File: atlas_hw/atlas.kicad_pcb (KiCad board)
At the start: 2 copper layers, 200 parts, among them J1 USB_C_Receptacle_USB2.0, J10 PSP_LCD, J2 DEBUG_STM, J3 PSP_TOUCH, J4 DEBUG_NRF, J5 CELL_THERM, J6 CELL_BARE, J7 AUX_THERM, J8 Micro_SD_Card_Det, J9 PSP_LCD_BL, Q1 Q_NMOS_DGS, Q2 Q_NMOS_DGS, Q3 Q_NMOS_DGS, Q4 Q_NMOS_DGS, Q5 Q_NMOS_DGS, SW1 SReset, SW2 Power, SW3 ResetSTM, SW4 ResetNRF, U1 STM32H723VITx, U10 BQ25611D, U11 STM6601CA2BDM6F, U12 BGA725L6, U13 LSF0108, U14 NPP600SNADJ, U15 TPS61073, U16 PAM2841, U17 NX3L1T3157, U2 W957A8MFYA5I, U3 MCP1811B, U4 TLV62569DBV, U5 nRF52810-QCxx, U6 LC709203F, U7 Teseo-LIV3F, U8 MS5637, U9 MC6470, Y1 16M, Y2 32k, Y3 32M, Y4 32k

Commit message: started layout
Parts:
- removed R45, R48, R49, R50, R51, R52, R53: NP, Resistor_SMD:R_0402_1005Metric
- removed U17: NX3L1T3157, Package_TO_SOT_SMD:SOT-886
- added RN5: R_Pack04, Resistor_SMD:R_Array_Concave_4x0402, F.Cu at (125.2, 40.9)
- added RN6: R_Pack04, Resistor_SMD:R_Array_Concave_4x0402, F.Cu at (128.3, 40.9)
- AE1: footprint Inductor_SMD:L_1206_3216Metric -> Resistor_SMD:R_1206_3216Metric
- J3, RN1, RN2, RN3, RN4, U1, U7: moved to B.Cu
- U12: value BGA725L6 -> BGU7007; footprint atlas:TSLP-6-2 -> atlas:6-XSON_1.5x1.0mm_0.5mm
- Y1, Y3: footprint Crystal:Crystal_SMD_2016-4Pin_2.0x1.6mm -> Crystal:Crystal_SMD_3225-4Pin_3.2x2.5mm
- Y2, Y4: footprint Crystal:Crystal_SMD_2012-2Pin_2.0x1.2mm -> Crystal:Crystal_SMD_3225-4Pin_3.2x2.5mm
- moved J8 154.1 mm to (257.3, 137.4), turned to 90 degrees
- moved U2 140.3 mm to (255.4, 124.7), turned to 270 degrees
- moved U10 137.7 mm to (233.8, 160.9)
- moved U5 129.4 mm to (252.9, 168.7), turned to 180 degrees
- moved J1 125.6 mm to (230.9, 175.2)
- moved AE2 124.4 mm to (206.6, 167.2), turned to 180 degrees
- moved U1 109.7 mm to (240.4, 129.8)
- moved U7 104.9 mm to (210.0, 157.8), turned to 180 degrees
- moved U13 96.7 mm to (241.1, 133.7)
- moved RN1 65.5 mm to (219.3, 136.7), turned to 0 degrees
- moved J10 64.6 mm to (223.1, 129.7)
- moved RN2 42.3 mm to (219.3, 132.7)
- moved RN3 39.3 mm to (219.3, 128.7)
- moved RN4 35.1 mm to (219.3, 125.2)
- moved J3 32.9 mm to (122.6, 139.0), turned to 270 degrees
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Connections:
- U12 pad 2: /GPS_VCC_RF -> GND
- U12 pad 3: Net-(F1-Pad1) -> Net-(L8-Pad1)
- U12 pad 4: GND -> /GPS_VCC_RF
- U12 pad 5: Net-(L8-Pad1) -> /GPS_ANT_OFF
- U12 pad 6: /GPS_ANT_OFF -> Net-(F1-Pad1)
- U6 pad 7: (no net) -> /I2C1_SCL_SYSTEM
- U6 pad 8: (no net) -> /I2C1_SCL_SYSTEM
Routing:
- net /SD_D1: track 0.00 -> 26.0 mm
- net /SD_D0: track 0.00 -> 24.5 mm
- net /SD_CLK: track 0.00 -> 24.2 mm
- net /OCTOSPIM_P1_NPLK: track 0.00 -> 22.2 mm, vias 0 -> 1
- net /SD_CMD: track 0.00 -> 21.4 mm
- net /SD_D3: track 0.00 -> 21.1 mm
- net /SD_D2: track 0.00 -> 20.9 mm
- net /OCTOSPIM_P1_NPS: track 0.00 -> 13.4 mm, vias 0 -> 1
- net /OCTOSPIM_P1_IO7: track 0.00 -> 11.9 mm, vias 0 -> 1
- net /OCTOSPIM_P1_IO6: track 0.00 -> 11.0 mm, vias 0 -> 1
- net /OCTOSPIM_P1_CLK: track 0.00 -> 10.7 mm, vias 0 -> 1
- net /OCTOSPIM_P1_IO5: track 0.00 -> 10.3 mm, vias 0 -> 1
- net /SDMMC1_D2: track 0.00 -> 8.88 mm, vias 0 -> 1
- net /OCTOSPIM_P1_IO4: track 0.00 -> 8.66 mm, vias 0 -> 1
- net /OCTOSPIM_P1_DQS: track 0.00 -> 8.44 mm, vias 0 -> 1
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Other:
- board outline added: 71 x 73.4 mm

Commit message: gps and other layout
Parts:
- removed J6: CELL_BARE, Connector_JST:JST_GH_SM02B-GHS-TB_1x02-1MP_P1.25mm_Horizontal
- removed J7: AUX_THERM, Connector_JST:JST_GH_SM02B-GHS-TB_1x02-1MP_P1.25mm_Horizontal
- C43, C45, C46, F1, J5, R12, R13, R14, R15, RN5, RN6, U12: moved to B.Cu
- J1: footprint Connector_USB:USB_C_Receptacle_Amphenol_12401548E4-2A -> Connector_USB:USB_C_Receptacle_Amphenol_12401610E4-2A
- L8: footprint Inductor_SMD:L_0603_1608Metric -> Inductor_SMD:L_0402_1005Metric; moved to B.Cu
- moved RN5 154.6 mm to (242.6, 141.6), turned to 180 degrees
- moved RN6 154.0 mm to (242.6, 144.1), turned to 180 degrees
- moved U6 136.3 mm to (255.3, 161.9), turned to 180 degrees
- moved J5 125.9 mm to (245.3, 152.6)
- moved C31 112.3 mm to (255.3, 158.5), turned to 180 degrees
- moved C46 110.8 mm to (203.6, 168.1), turned to 180 degrees
- moved C27 105.3 mm to (232.8, 168.6)
- moved L3 99.2 mm to (143.8, 174.0), turned to 180 degrees
- moved R13 95.0 mm to (232.7, 171.1)
- moved R14 94.9 mm to (231.4, 166.3), turned to 270 degrees
- moved R12 93.1 mm to (228.9, 171.1)
- moved R16 93.0 mm to (231.4, 166.3), turned to 270 degrees
- moved C13 92.7 mm to (147.3, 169.4)
- moved R17 91.4 mm to (230.4, 166.3), turned to 270 degrees
- moved L2 91.3 mm to (208.0, 128.8), turned to 90 degrees
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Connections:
- J10 pad 1: GND -> Net-(J10-Pad1)
- J10 pad 10: /LTDC_R5 -> /LTDC_DE
- J10 pad 11: /LTDC_R6 -> /LTDC_CK
- J10 pad 12: /LTDC_R7 -> GND
- J10 pad 13: /LTDC_G4 -> /LTDC_B7
- J10 pad 14: /LTDC_G5 -> /LTDC_B6
- J10 pad 15: /LTDC_G6 -> /LTDC_B5
- J10 pad 16: /LTDC_G7 -> /LTDC_B4
- J10 pad 17: /LTDC_G4 -> /LTDC_B7
- J10 pad 18: /LTDC_G5 -> /LTDC_B6
- J10 pad 19: /LTDC_G6 -> /LTDC_B5
- J10 pad 2: GND -> Net-(J10-Pad2)
- J10 pad 20: /LTDC_G7 -> /LTDC_B4
- J10 pad 21: /LTDC_B4 -> /LTDC_G7
- J10 pad 22: /LTDC_B5 -> /LTDC_G6
- J10 pad 23: /LTDC_B6 -> /LTDC_G5
- J10 pad 24: /LTDC_B7 -> /LTDC_G4
- J10 pad 25: /LTDC_B4 -> /LTDC_G7
- J10 pad 26: /LTDC_B5 -> /LTDC_G6
- J10 pad 27: /LTDC_B6 -> /LTDC_G5
- J10 pad 28: /LTDC_B7 -> /LTDC_G4
- J10 pad 29: GND -> /LTDC_R7
- J10 pad 3: Net-(C54-Pad1) -> Net-(J10-Pad3)
- J10 pad 30: /LTDC_CK -> /LTDC_R6
- J10 pad 31: /LTDC_DE -> /LTDC_R5
- J10 pad 32: /LTDC_HS -> /LTDC_R4
- J10 pad 33: /LTDC_VS -> /LTDC_R7
- J10 pad 34: Net-(J10-Pad34) -> /LTDC_R6
- J10 pad 35: Net-(C51-Pad1) -> /LTDC_R5
- J10 pad 36: Net-(J10-Pad36) -> /LTDC_R4
- J10 pad 37: Net-(J10-Pad37) -> Net-(C54-Pad1)
- J10 pad 38: Net-(J10-Pad38) -> Net-(C54-Pad1)
- J10 pad 39: Net-(J10-Pad39) -> GND
- J10 pad 4: Net-(C54-Pad1) -> Net-(J10-Pad4)
- J10 pad 40: Net-(J10-Pad40) -> GND
- J10 pad 5: /LTDC_R4 -> Net-(J10-Pad5)
- J10 pad 6: /LTDC_R5 -> Net-(C51-Pad1)
- J10 pad 7: /LTDC_R6 -> Net-(J10-Pad7)
- J10 pad 8: /LTDC_R7 -> /LTDC_VS
- J10 pad 9: /LTDC_R4 -> /LTDC_HS
- R82 pad 2: Net-(J10-Pad38) -> Net-(J10-Pad3)
- R83 pad 2: Net-(J10-Pad39) -> Net-(J10-Pad2)
- R84 pad 2: Net-(J10-Pad40) -> Net-(J10-Pad1)
- RN1 pad 1: GND -> /LTDC_R4
- RN1 pad 2: GND -> /LTDC_R5
- RN1 pad 3: GND -> /LTDC_R6
- RN1 pad 4: GND -> /LTDC_R7
- RN1 pad 5: /LTDC_R7 -> GND
- RN1 pad 6: /LTDC_R6 -> GND
- RN1 pad 7: /LTDC_R5 -> GND
- RN1 pad 8: /LTDC_R4 -> GND
- RN2 pad 1: GND -> /LTDC_G4
- RN2 pad 2: GND -> /LTDC_G5
- RN2 pad 3: GND -> /LTDC_G6
- RN2 pad 4: GND -> /LTDC_G7
- RN2 pad 5: /LTDC_G7 -> GND
- RN2 pad 6: /LTDC_G6 -> GND
- RN2 pad 7: /LTDC_G5 -> GND
- RN2 pad 8: /LTDC_G4 -> GND
- RN3 pad 1: GND -> /LTDC_B4
- RN3 pad 2: GND -> /LTDC_B5
- RN3 pad 3: GND -> /LTDC_B6
- RN3 pad 4: GND -> /LTDC_B7
- RN3 pad 5: /LTDC_B7 -> GND
- RN3 pad 6: /LTDC_B6 -> GND
- RN3 pad 7: /LTDC_B5 -> GND
- RN3 pad 8: /LTDC_B4 -> GND
- RN4 pad 1: GND -> /LTDC_CK
- RN4 pad 2: GND -> /LTDC_DE
- RN4 pad 3: GND -> /LTDC_HS
- RN4 pad 4: GND -> /LTDC_VS
- RN4 pad 5: /LTDC_VS -> GND
- RN4 pad 6: /LTDC_HS -> GND
- RN4 pad 7: /LTDC_DE -> GND
- RN4 pad 8: /LTDC_CK -> GND
- RN5 pad 1: /SDMMC1_D2 -> /SD_D2
- RN5 pad 2: /SDMMC1_D3 -> /SD_D3
- RN5 pad 3: /SDMMC1_CMD -> /SD_CMD
- RN5 pad 4: /SDMMC1_CK -> /SD_CLK
- RN5 pad 5: /SD_CLK -> /SDMMC1_CK
- RN5 pad 6: /SD_CMD -> /SDMMC1_CMD
- RN5 pad 7: /SD_D3 -> /SDMMC1_D3
- RN5 pad 8: /SD_D2 -> /SDMMC1_D2
- RN6 pad 1: /SDMMC1_D0 -> /SD_D0
- RN6 pad 2: /SDMMC1_D1 -> /SD_D1
- RN6 pad 7: /SD_D1 -> /SDMMC1_D1
- RN6 pad 8: /SD_D0 -> /SDMMC1_D0
- U6 pad : (no net) -> GND
- U7 pad 10: Net-(C43-Pad2) -> GND
- U7 pad 11: (no net) -> Net-(C43-Pad2)
- U7 pad 18: (no net) -> Net-(U7-Pad18)
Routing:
- net /LTDC_R5: track 0.00 -> 43.7 mm, vias 0 -> 4
- net /LTDC_R4: track 0.00 -> 41.6 mm, vias 0 -> 4
- net /LTDC_R6: track 0.00 -> 39.4 mm, vias 0 -> 4
- net /LTDC_B7: track 0.00 -> 38.7 mm, vias 0 -> 4
- net /LTDC_VS: track 0.00 -> 37.8 mm, vias 0 -> 4
- net /LTDC_G7: track 0.00 -> 37.1 mm, vias 0 -> 4
- net /LTDC_R7: track 0.00 -> 36.2 mm, vias 0 -> 4
- net /LTDC_HS: track 0.00 -> 36.2 mm, vias 0 -> 2
- net /LTDC_B5: track 0.00 -> 35.6 mm, vias 0 -> 4
- net /LTDC_G5: track 0.00 -> 35.6 mm, vias 0 -> 4
- net /LTDC_B4: track 0.00 -> 35.3 mm, vias 0 -> 4
- net /LTDC_G4: track 0.00 -> 35.1 mm, vias 0 -> 4
- net /LPUART1_TX_GPS: track 0.00 -> 34.9 mm
- net /LPUART1_RX_GPS: track 0.00 -> 34.5 mm
- net /LTDC_B6: track 0.00 -> 33.5 mm, vias 0 -> 3
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- added copper zone on B.Cu, net GND
- added copper zone on F.Cu, net GND
- added copper zone on In1.Cu, net GND
- added copper zone on In2.Cu, net GND
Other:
- outline, holes or cut-outs redrawn
- copper layers 2 -> 4

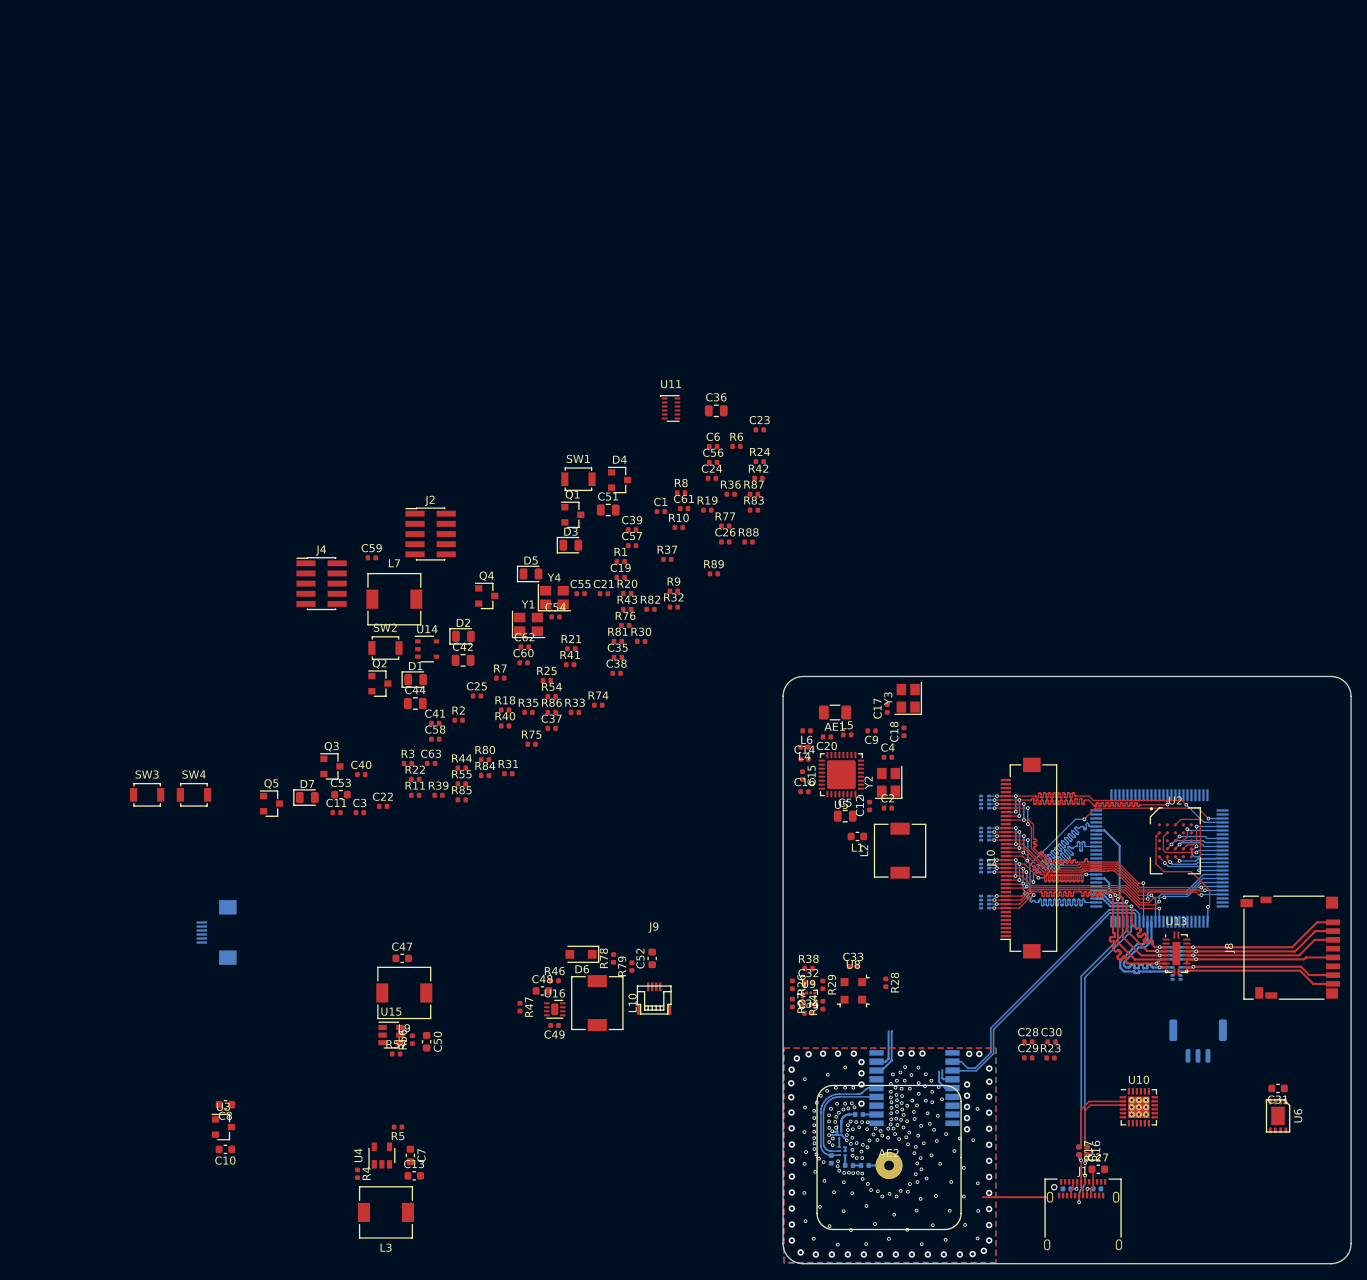
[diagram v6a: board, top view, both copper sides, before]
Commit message: stripped back design to basics
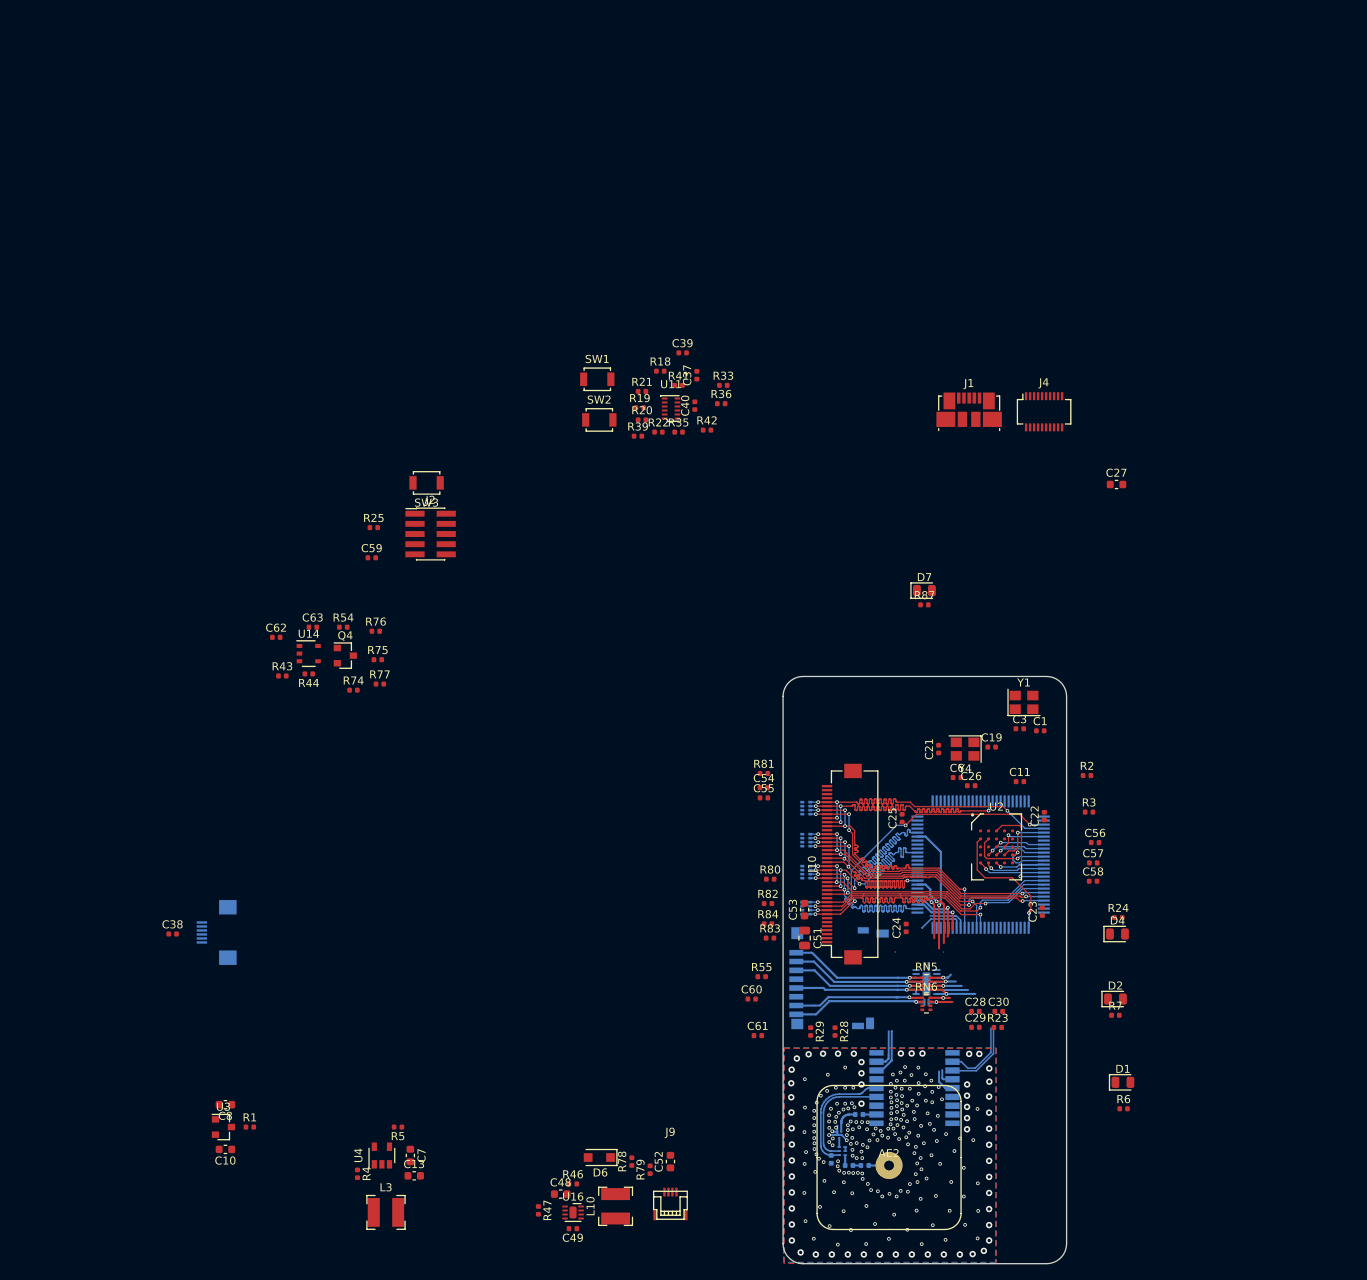
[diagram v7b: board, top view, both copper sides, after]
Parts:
- removed AE1: CHIP, Resistor_SMD:R_1206_3216Metric
- removed C12: 100p, Capacitor_SMD:C_0402_1005Metric
- removed C14, C17, C18: 1p, Capacitor_SMD:C_0402_1005Metric
- removed C15: NP, Capacitor_SMD:C_0402_1005Metric
- removed C16, C32, C33, C34, C35, C9: 0.1u, Capacitor_SMD:C_0402_1005Metric
- removed C2, C4: 12p, Capacitor_SMD:C_0402_1005Metric
- removed C20: 2.2p, Capacitor_SMD:C_0402_1005Metric
- removed C31, C47, C50: 1u, Capacitor_SMD:C_0603_1608Metric
- removed C36, C42, C44, C5: 10u, Capacitor_SMD:C_0805_2012Metric
- removed C41: 47n, Capacitor_SMD:C_0402_1005Metric
- removed D3: NRF_STATUS, LED_SMD:LED_0805_2012Metric
- removed D5: CHARGE_STATUS, LED_SMD:LED_0805_2012Metric
- removed J5: CELL_THERM, Connector_JST:JST_GH_SM03B-GHS-TB_1x03-1MP_P1.25mm_Horizontal
- removed L1: 3.9n, Inductor_SMD:L_0603_1608Metric
- removed L2: 15u, Inductor_SMD:L_6.3x6.3_H3
- removed L4, L6: 3.9n, Inductor_SMD:L_0402_1005Metric
- removed L5: NP, Inductor_SMD:L_0402_1005Metric
- removed L7: 1u, Inductor_SMD:L_6.3x6.3_H3
- removed L9: L_Small, Inductor_SMD:L_6.3x6.3_H3
- removed Q1, Q2, Q3, Q5: Q_NMOS_DGS, Package_TO_SOT_SMD:SOT-23
- removed R10, R11, R37, R9: 1k, Resistor_SMD:R_0402_1005Metric
- removed R12, R13: 5.1k, Resistor_SMD:R_0402_1005Metric
- removed R14, R15, R16, R17, R40, R88, R89: 0, Resistor_SMD:R_0402_1005Metric
- removed R26, R27, R56, R57: NP, Resistor_SMD:R_0402_1005Metric
- removed R30: 10k, Resistor_SMD:R_0402_1005Metric
- removed R31, R32, R34, R38, R8, R85, R86: 100k, Resistor_SMD:R_0402_1005Metric
- removed SW4: ResetNRF, Button_Switch_SMD:SW_SPST_B3U-1000P
- removed U10: BQ25611D, Package_DFN_QFN:WQFN-24-1EP_4x4mm_P0.5mm_EP2.7x2.7mm_ThermalVias
- removed U15: TPS61073, Package_TO_SOT_SMD:SOT-23-6
- removed U5: nRF52810-QCxx, Package_DFN_QFN:QFN-32-1EP_5x5mm_P0.5mm_EP3.6x3.6mm
- removed U6: LC709203F, atlas:WDFN-8_3x4mm_0.6mm_1.96x2.56mm
- removed U8: MS5637, atlas:QFN-4_3x3_Pitch2mm
- removed U9: MC6470, Package_LGA:LGA-12_2x2mm_P0.5mm
- removed Y2: 32k, Crystal:Crystal_SMD_3225-4Pin_3.2x2.5mm
- removed Y3: 32M, Crystal:Crystal_SMD_3225-4Pin_3.2x2.5mm
- D4: value DC -> MCU_ON; footprint Package_TO_SOT_SMD:SOT-23 -> LED_SMD:LED_0805_2012Metric
- J1: value USB_C_Receptacle_USB2.0 -> USB_B_Micro; footprint Connector_USB:USB_C_Receptacle_Amphenol_12401610E4-2A -> Connector_USB:USB_Micro-B_Molex_47346-0001
- J4: value DEBUG_NRF -> Conn_02x10_Counter_Clockwise; footprint Connector_PinHeader_1.27mm:PinHeader_2x05_P1.27mm_Vertical_SMD -> Connector_Molex:Molex_SlimStack_55560-0201_2x10_P0.50mm_Vertical
- J8, U13: moved to B.Cu
- L10, L3: footprint Inductor_SMD:L_6.3x6.3_H3 -> Inductor_SMD:L_Bourns-SRN4018
- R24: value 0 -> 1k
- R6, R7: value 100k -> 1k
- RN5, RN6: moved to F.Cu
- moved J1 102.5 mm to (216.7, 73.7)
- moved D1 101.7 mm to (235.9, 157.7)
- moved R6 95.9 mm to (236.0, 161.0)
- moved D2 93.3 mm to (234.9, 147.3)
- moved J4 92.8 mm to (226.0, 73.9)
- moved R7 87.7 mm to (234.9, 149.4)
- moved C27 85.6 mm to (235.1, 83.0)
- moved C11 85.5 mm to (223.0, 120.1)
- moved R3 85.4 mm to (231.6, 124.0)
- moved R1 84.5 mm to (126.7, 163.3)
- moved D4 84.2 mm to (235.2, 139.2)
- moved C58 84.1 mm to (232.2, 132.6)
- moved C3 83.2 mm to (223.0, 113.5)
- moved C22 82.7 mm to (226.1, 124.5), turned to 90 degrees
- moved D7 81.4 mm to (211.1, 96.3)
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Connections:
- C39 pad 1: /VCC_SYS -> /USB_PORT_VBUS
- C7 pad 1: /VCC_SYS -> /USB_PORT_VBUS
- C8 pad 2: /VCC_SYS -> /USB_PORT_VBUS
- D1 pad 2: /VCC_MCU_3V3 -> /GPS_1PPS
- D2 pad 2: /VCC_MCU_3V3 -> /STM_STATUS
- D4 pad 1: /DEBUG_NRESET_STM -> Net-(D4-Pad1)
- D4 pad 2: /DEBUG_NRESET_NRF -> /VCC_MCU_3V3
- J3 pad 1: /I2C1_SCL_SYSTEM -> /I2C_SCL_SENSOR
- J3 pad 2: /I2C1_SCL_SYSTEM -> /I2C_SDA_SENSOR
- J4 pad 1: /VCC_MCU_3V3 -> Net-(J4-Pad1)
- J4 pad 10: /DEBUG_NRESET_NRF -> Net-(J4-Pad10)
- J4 pad 2: /DEBUG_SWDIO_NRF -> Net-(J4-Pad2)
- J4 pad 3: GND -> Net-(J4-Pad3)
- J4 pad 4: /DEBUG_SWDCLK_NRF -> Net-(J4-Pad4)
- J4 pad 5: GND -> Net-(J4-Pad5)
- J4 pad 9: GND -> Net-(J4-Pad9)
- R24 pad 1: GND -> Net-(D4-Pad1)
- R24 pad 2: Net-(R24-Pad2) -> GND
- R36 pad 2: /PWR_MCU_NRST -> /DEBUG_NRESET_STM
- R46 pad 2: /VCC_SYS -> /USB_PORT_VBUS
- R6 pad 1: /GPS_1PPS -> Net-(D1-Pad1)
- R7 pad 1: /STM_STATUS -> Net-(D2-Pad1)
- R80 pad 2: /VCC_LCD_PWR -> /VCC_VBUS_USB
- U1 pad 1: /SP4_SCK_NRF -> Net-(U1-Pad1)
- U1 pad 16: /BTN_ENTER -> /BTN_UP
- U1 pad 17: /BTN_DOWN -> /BTN_RIGHT
- U1 pad 18: /BTN_LEFT -> /BTN_DOWN
- U1 pad 2: /NRF_INT -> Net-(U1-Pad2)
- U1 pad 23: /LC709203_INT -> Net-(U1-Pad23)
- U1 pad 24: /BTN_UP -> Net-(U1-Pad24)
- U1 pad 25: /BTN_RIGHT -> Net-(U1-Pad25)
- U1 pad 3: /~USB_DET -> Net-(U1-Pad3)
- U1 pad 32: Net-(U1-Pad32) -> /BTN_LEFT
- U1 pad 4: /SP4_MISO_NRF -> Net-(U1-Pad4)
- U1 pad 5: /SP4_MOSI_NRF -> Net-(U1-Pad5)
- U1 pad 55: /MC6470_INTA -> Net-(U1-Pad55)
- U1 pad 56: /MC6470_INTM -> Net-(U1-Pad56)
- U1 pad 7: /BQ25611_INT -> Net-(U1-Pad7)
- U1 pad 85: /EN_SD_PWR -> /PWR_MCU_INT
- U1 pad 86: /PWR_MCU_HOLD -> /PWR_BTN_OUT
- U1 pad 87: /PWR_BTN_OUT -> /PWR_MCU_HOLD
- U1 pad 88: /PWR_MCU_INT -> Net-(U1-Pad88)
- U1 pad 93: /I2C1_SCL_SYSTEM -> /I2C1_SDA_SYSTEM
- U1 pad 97: /UART8_RX_NRF -> Net-(U1-Pad97)
- U1 pad 98: /UART8_TX_NRF -> Net-(U1-Pad98)
- U11 pad 1: /VCC_SYS -> /USB_PORT_VBUS
- U11 pad 10: /PWR_MCU_NRST -> /DEBUG_NRESET_STM
- U13 pad 18: Net-(R89-Pad1) -> GND
- U13 pad 3: Net-(R88-Pad1) -> GND
- U3 pad 1: /VCC_SYS -> /USB_PORT_VBUS
- U4 pad 4: /VCC_SYS -> /USB_PORT_VBUS
- U7 pad 10: GND -> Net-(C43-Pad2)
- U7 pad 11: Net-(C43-Pad2) -> (no net)
- U7 pad 18: Net-(U7-Pad18) -> (no net)
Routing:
- net /USB_STM_D-: track 30.7 -> 0.00 mm
- net /USB_STM_D+: track 30.7 -> 0.61 mm
- net /LPUART1_TX_GPS: track 34.9 -> 14.0 mm
- net /LPUART1_RX_GPS: track 34.5 -> 15.5 mm
- net /SDMMC1_D0: track 16.1 -> 3.26 mm
- net /SDMMC1_D1: track 16.4 -> 3.78 mm
- net /USB_CHGR_D+: track 10.7 -> 0.00 mm
- net /USB_CHGR_D-: track 9.98 -> 0.00 mm
- net /USB_PORT_D-: track 9.04 -> 0.00 mm, vias 3 -> 0
- net GND: track 13.2 -> 4.76 mm
- net /SDMMC1_CK: track 21.8 -> 14.2 mm
- net /SDMMC1_D2: track 17.2 -> 10.6 mm
- net /USB_PORT_D+: track 6.10 -> 0.00 mm, vias 1 -> 0
- net /USB_PORT_VBUS: track 5.20 -> 0.19 mm
- net /SDMMC1_D3: track 15.9 -> 12.2 mm
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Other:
- board size 71 x 73.4 mm -> 35.4 x 73.4 mm
